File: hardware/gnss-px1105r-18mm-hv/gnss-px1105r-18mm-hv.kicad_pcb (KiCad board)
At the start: 6 copper layers, 22 x 30 mm, 49 parts, among them J3 BM05B-SRSS-TB, U1 PX1105R, U2 ADP7142ARDZ-3.3, U3 BGA855N6, U4 BGA855N6, U5 LP5907MFX-1.8

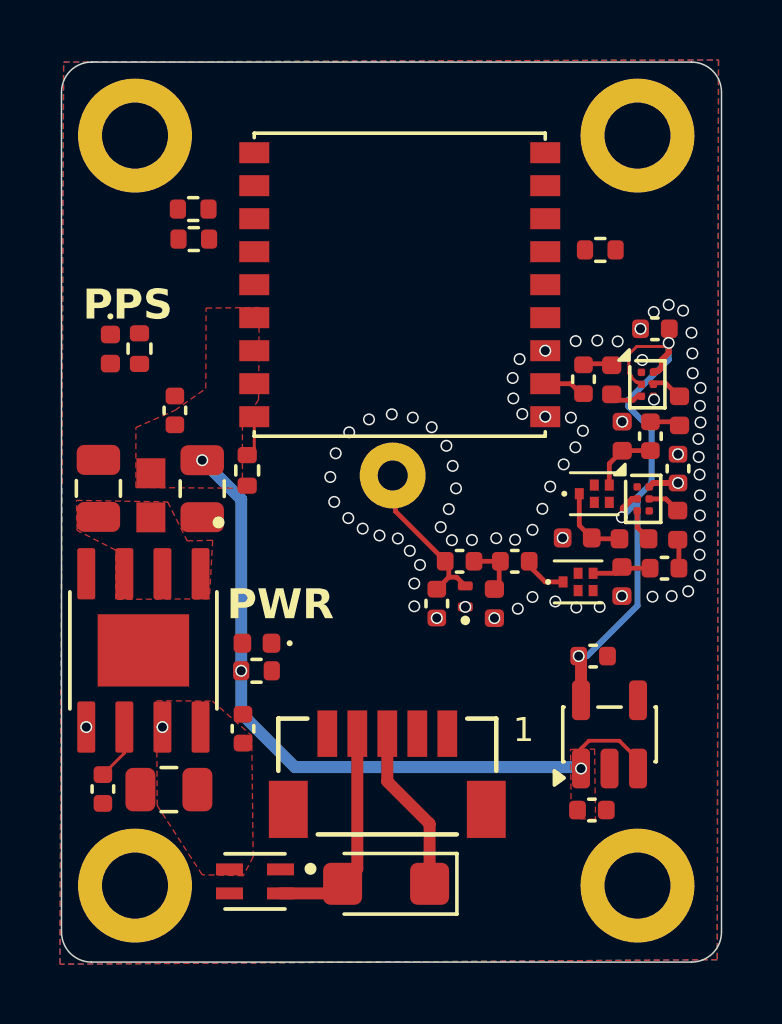
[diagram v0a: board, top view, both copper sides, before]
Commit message: hardware(gnss-px1105r): the carrier routed and its DRC errors fixed -- the GND vias moved clear of L7's RF pads and U4's AO pin, U4's +1V8 pins clear of the RF tracks, R3/D3 apart; no clearance errors and nothing unconnected
DRC with the zones refilled now leaves only warnings: four footprints that differ from their library copies (U2, R1, R2, D1, carried over from the SAM carrier) and three silkscreen overlaps (U3/FL5, U2/C1, U4/L8).

Co-Authored-By: Claude Opus 5.5 <noreply@anthropic.com>
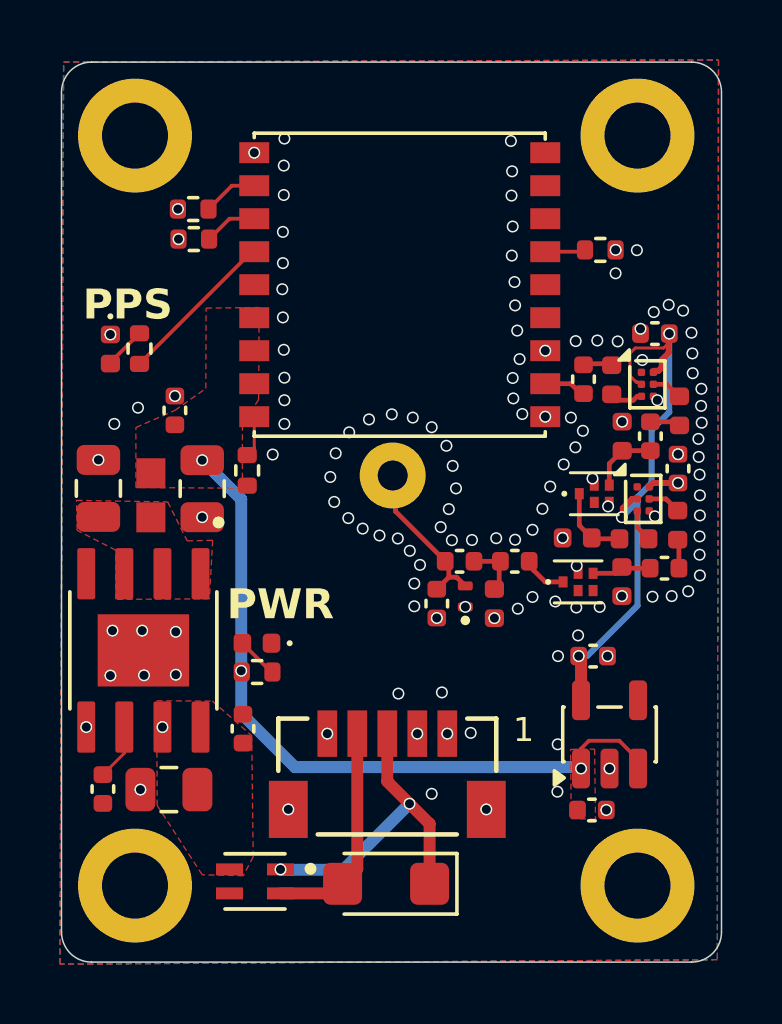
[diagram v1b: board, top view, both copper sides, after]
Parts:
- moved C25 0.16 mm to (61.9, 36.1)
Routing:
- net Net-(J3-Pad5): track 0.00 -> 45.1 mm, vias 0 -> 2
- net Net-(J3-Pad2): track 0.00 -> 21.1 mm, vias 0 -> 2
- net Net-(J3-Pad1): track 0.00 -> 20.2 mm, vias 0 -> 2
- net Net-(U1-PPS): track 0.00 -> 5.37 mm
- net VSYS: track 5.59 -> 10.8 mm, vias 0 -> 2
- net GNSS_TX: track 0.00 -> 1.85 mm
- net GNSS_RX: track 0.00 -> 1.79 mm
- net Net-(D1-A): track 0.00 -> 1.41 mm
- net Net-(D3-A): track 0.00 -> 1.40 mm
- net RXD2: track 0.00 -> 1.35 mm
- net GND: vias 76 -> 129

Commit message: hardware(gnss-px1105r): V1 release -- 4 layers on a 1.2 mm JLC04121H-3313 board, no via-in-pad, and its fabrication notes
The prototype carrier, as ordered:
- Stackup JLC04121H-3313 (3313 0.0994 / core 0.865 / 3313 0.0994), 1.2 mm. The top prepreg is unchanged, so the
  0.16 mm RF traces stay 50 ohm; the GVLB208.A's 1.2 mm feed pin now ends about flush with the top copper
  (review K1).
- No via-in-pad: every via is out of the SMD lands and its copper at least 0.09 mm from any mask opening,
  including U3/U4's single mask windows; vias tented, no fill or cap. The supply routes are off B.Cu under the
  patch; two dangling B.Cu stubs removed.
- U1 pin-1 dot and F.Fab outline, U2's dot off C1's pad (review L1); fiducials FID1-FID3, board-only (L6);
  U1 pin 18 no-connect flag, ERC 0 errors (S4); AE1 feed pad 1.4 mm on the antenna side and inner layers, a
  0.20 mm ring (S5).
- FABRICATION-NOTES.md (review D1, D2, K1): stackup, vias, 80 um stencil, reflow and MSL limits, U2 fixed 3.3 V
  only, placement checks, the antenna's hand fit and staking. Paste convention row added.
- The design review of 2026-10-12.

DRC 0 errors, 0 unconnected, 0 parity (5 old library/silk warnings); check_board_parity.py passes.

Co-Authored-By: Claude Opus 5.5 <noreply@anthropic.com>
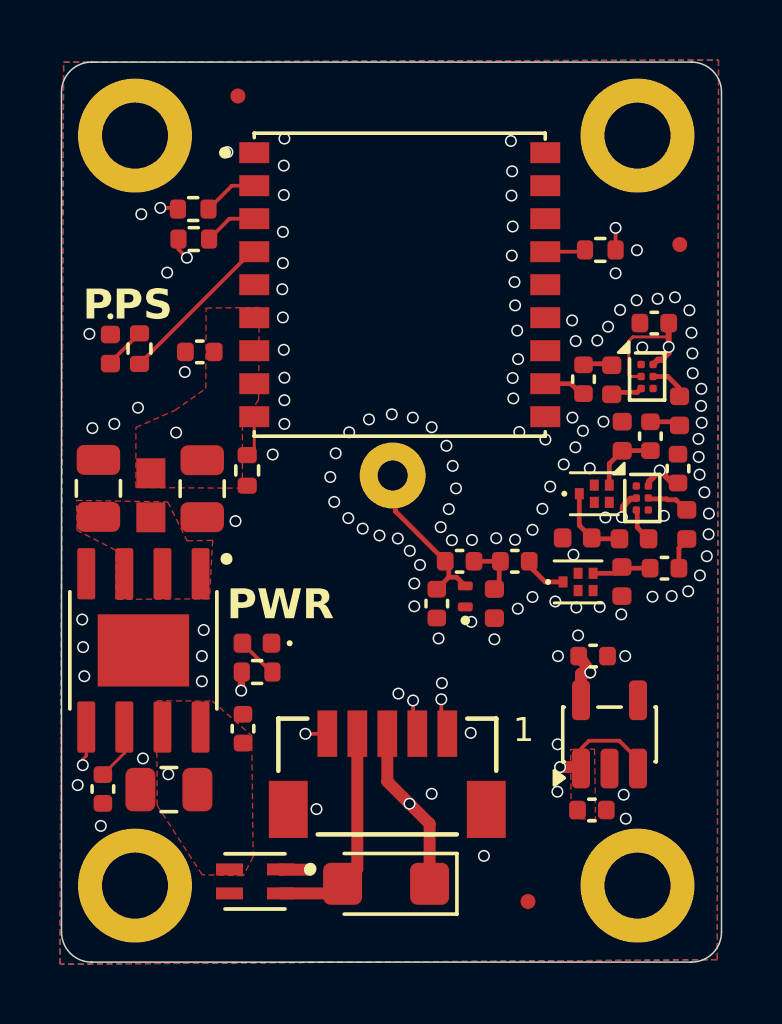
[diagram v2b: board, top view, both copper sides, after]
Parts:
- added FID1: Fiducial_0.5mm_Mask1mm, Fiducial:Fiducial_0.5mm_Mask1mm, F.Cu at (48.0, 28.2)
- added FID2: Fiducial_0.5mm_Mask1mm, Fiducial:Fiducial_0.5mm_Mask1mm, F.Cu at (57.7, 55.0)
- added FID3: Fiducial_0.5mm_Mask1mm, Fiducial:Fiducial_0.5mm_Mask1mm, F.Cu at (62.8, 33.1)
- moved C5 2.12 mm to (46.8, 36.7), turned to 180 degrees
- moved C25 0.35 mm to (61.9, 35.7)
- moved L3 0.30 mm to (63.0, 42.5)
- moved U4 0.26 mm to (61.7, 37.5)
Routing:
- net Net-(U2-EN): track 2.54 -> 4.37 mm
- net +3V3: track 24.3 -> 26.1 mm
- net Net-(J3-Pad5): track 45.1 -> 46.6 mm
- net Net-(J3-Pad2): track 21.1 -> 22.1 mm
- net +1V8: track 21.9 -> 22.7 mm
- net GND: vias 129 -> 131
- removed copper zone on In3.Cu, net GND
- removed copper zone on In4.Cu, net GND
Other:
- copper layers 6 -> 4
